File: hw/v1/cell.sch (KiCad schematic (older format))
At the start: 40 parts, among them Q201 Q_NMOS_GDS, Q202 Q_NMOS_GDS, Q203 Q_NMOS_GDS, U201 OPA1604, U202 ZTP-135SR

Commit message: Progress with the schema and PCB....
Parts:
- removed C209: 10n, Capacitor_SMD:C_0603_1608Metric, symbol Device:C_Small
- removed C210: 100n, Capacitor_SMD:C_0603_1608Metric, symbol Device:C_Small
- removed R213: 150, Resistor_SMD:R_0603_1608Metric, symbol Device:R_Small
- removed R215: 2k, Resistor_SMD:R_0603_1608Metric, symbol Device:R_Small
- removed U201: OPA1604, Package_SO:SOIC-16_3.9x9.9mm_P1.27mm, symbol Amplifier_Operational:OPA1604
- removed U202: ZTP-135SR, Package_TO_SOT_THT:TO-46-4_Window, symbol Cell_Shaper:ZTP-135SR
- added C209: 100n, Capacitor_SMD:C_0603_1608Metric, symbol Device:C
- added R218: 100k, Resistor_SMD:R_0603_1608Metric, symbol Device:R_Small
- added R219: 10k, Resistor_SMD:R_0603_1608Metric, symbol Device:R_Small
- added R220: 0, Resistor_SMD:R_0603_1608Metric, symbol Device:R
- added U201: MCP1416, Package_TO_SOT_SMD:SOT-23-5, symbol Driver_FET:MCP1416
- added U202: LMV344IPWR, Package_SO:TSSOP-14_4.4x5mm_P0.65mm, symbol Amplifier_Operational:LMV324
- C201, C202: value 10u -> 10u 16V
- C204: renamed from C203; value 10u -> 22u
- C205: renamed from C204; value 1u -> 10u
- C206: renamed from C205; DNP (none) -> DNP
- C207, C208: DNP (none) -> DNP
- D203: renamed from D202; value D_Schottky -> DFLS230Q; footprint Diode_SMD:D_0603_1608Metric -> Diode_SMD:D_PowerDI-123
- L201: value 10u -> 100u; footprint Inductor_SMD:L_Vishay_IHLP-2525 -> Inductor_SMD:L_Wuerth_HCI-7050
- Q201: value Q_NMOS_GDS -> ZVN4206G; footprint Package_TO_SOT_SMD:SOT-223 -> Package_TO_SOT_SMD:SOT-223-3_TabPin2
- Q202, Q203: value Q_NMOS_GDS -> IRFZ24NPbF
- R203: renamed from R201; value R -> 10k
- R204: renamed from R202; value 1k -> 22k 0.5%
- R205: renamed from R203; value 1k -> 1k 0.5%
- R206: renamed from R204; value 0R1 -> 0R1 1%; footprint Resistor_SMD:R_1210_3225Metric -> Resistor_SMD:R_1206_3216Metric
- R207: renamed from R205; value 1k -> 1k 0.5%
- R208: renamed from R219; value 1k -> 22k 0.5%
- R209: renamed from R218; value R -> 10k
- R210: renamed from R206; value 0R1 -> 0R1 1%; footprint Resistor_SMD:R_1210_3225Metric -> Resistor_SMD:R_1206_3216Metric
- R211: renamed from R208; value 1k -> 1k 0.5%
- R212: renamed from R209; value 1k -> 1k 0.5%
- R213: renamed from R207; value 1k -> 100
- R214: renamed from R210; value 1k -> 200k
- R215: renamed from R211; DNP (none) -> DNP
- R216: renamed from R212; value 1k -> 22k 0.5%
- R217: renamed from R214; value 18k -> 1k
- TH201: footprint (none) -> CellShaper:ContactThermistor
- renumbered C206 to C203, D203 to D202, R216 to R201, R217 to R202
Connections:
- net labels added: CELL_POSITIVE, GATE, GNDPWR
- net labels removed: CELL
- wire segments 114 -> 120
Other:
- note added: "1A = 2.3V"
- note added: "? mA/mV"
- note added: "Cell temperature"
- note added: "Charge current\nmeasurement"
- note added: "Max 5V"
- note added: "TODO: Is it possible to make 4-wire voltage measurement? \nNow possible voltage difference between\nGND and PWR GND is added to measurement!\n\nChange opamp VCC to regulated 5V and use opamp\nas differential amp and have divider on output?"
- note added: "TODO: Single two-color LED?"
- note added: "Up to 2A and 12V"
- note added: "Wire leaded NTC\non a foam pad"
- note removed: "(Opamp is not really needed but\nquad packaged opamps are so common)"
- note removed: "Cel temperature"
- note removed: "Charge current measurement"
- note removed: "If DAC is used no filtering here!"
- moved on the sheet: BT201, C201, C202, C203, C204, C205, C206, C207, C208, D201, D202, D203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

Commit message: Progress...
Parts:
- added R221, R222: 300k 0.5%, Resistor_SMD:R_0603_1608Metric, symbol Device:R_Small
- added R223: 100k 0.5%, Resistor_SMD:R_0603_1608Metric, symbol Device:R_Small
- R214: value 200k -> 100k 0.5%
- R218: value 100k -> 100k 0.5%
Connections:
- net CELL_POSITIVE: now also R221.1; no longer R218.1
- net CELL_VOLTAGE: now also R218.1; no longer U202.2 (-)
- net GND: now also R214.1, R223.1
- net GNDPWR: now also R222.1; no longer R214.2
- net at C207.2, R211.2, U202.5 (+): now also R223.2
- new net: R214.2, R221.2, U202.3 (+)
- new net: R218.2, R222.2, U202.2 (-)
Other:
- note added: "3.3V --> 1.6A\n? mA/mV"
- note added: "Difference amplifier"
- note added: "Discharge current control"
- note added: "gain = 0.33333"
- note removed: "? mA/mV"
- note removed: "TODO: Is it possible to make 4-wire voltage measurement? \nNow possible voltage difference between\nGND and PWR GND is added to measurement!\n\nChange opamp VCC to regulated 5V and use opamp\nas differential amp and have divider on output?"
- moved on the sheet: R314, R318, U302A

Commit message: Soon...
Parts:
- added NT501: Net-Tie_2, NetTie:NetTie-2_SMD_Pad0.5mm, symbol Device:Net-Tie_2
- L201: footprint Inductor_SMD:L_Wuerth_HCI-7050 -> Inductor_SMD:L_Wuerth_HCM-1052
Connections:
- net CELL_VOLTAGE: now also U202.14; no longer U202.1
- net CHARGE_CURRENT: now also U202.1; no longer U202.14
- net GNDPWR: now also NT501.1; no longer R222.1
- net at C206.1, R204.2, R207.1: now also U202.2 (-); no longer U202.13 (-)
- net at C206.2, R205.1, R208.2: now also U202.3 (+); no longer U202.12 (+)
- net at R214.2, R221.2: now also U202.12 (+); no longer U202.3 (+)
- net at R218.2, R222.2: now also U202.13 (-); no longer U202.2 (-)
- new net: NT501.2, R222.1
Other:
- moved on the sheet: R221, R222, U202A, U202D

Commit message: Soooooon...
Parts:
- added R19, R5: 200m 1%, Resistor_SMD:R_1206_3216Metric, symbol Device:R
- R20: renamed from R210; value 0R1 1% -> 200m 1%
- R6: renamed from R206; value 0R1 1% -> 200m 1%
- renumbered BT201 to BT1, C201 to C1, C202 to C2, C204 to C3, C205 to C4, C206 to C5, C208 to C6, C209 to C7, C207 to C8, C203 to C9, D203 to D1, D201 to D2, D202 to D3, L201 to L1, NT501 to NT5, Q201 to Q1, Q203 to Q2, Q202 to Q3, R214 to R1, R213 to R10, R219 to R11, R220 to R12, R215 to R13, R208 to R14, R204 to R15, R203 to R16, R223 to R17, R211 to R18, R221 to R2, R212 to R21, R216 to R22, R209 to R23, R201 to R24, R202 to R25, R222 to R3, R218 to R4, R205 to R7, R207 to R8, R217 to R9, TH201 to TH1, U202 to U1, U201 to U2
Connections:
- net CELL_POSITIVE: now also R5.2
- net GNDPWR: now also R19.2
- net at Q2.3 (S), Q3.3 (S), R18.1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: now also R19.1
- net at C3.1, C4.1, L1.2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: now also R5.1
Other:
- note added: "Charge current shunt\n2x 200m or 1x 100m"
- note added: "Discharge current shunt\n2x 200m or 1x 100m"
- note removed: "Charge current\nmeasurement"

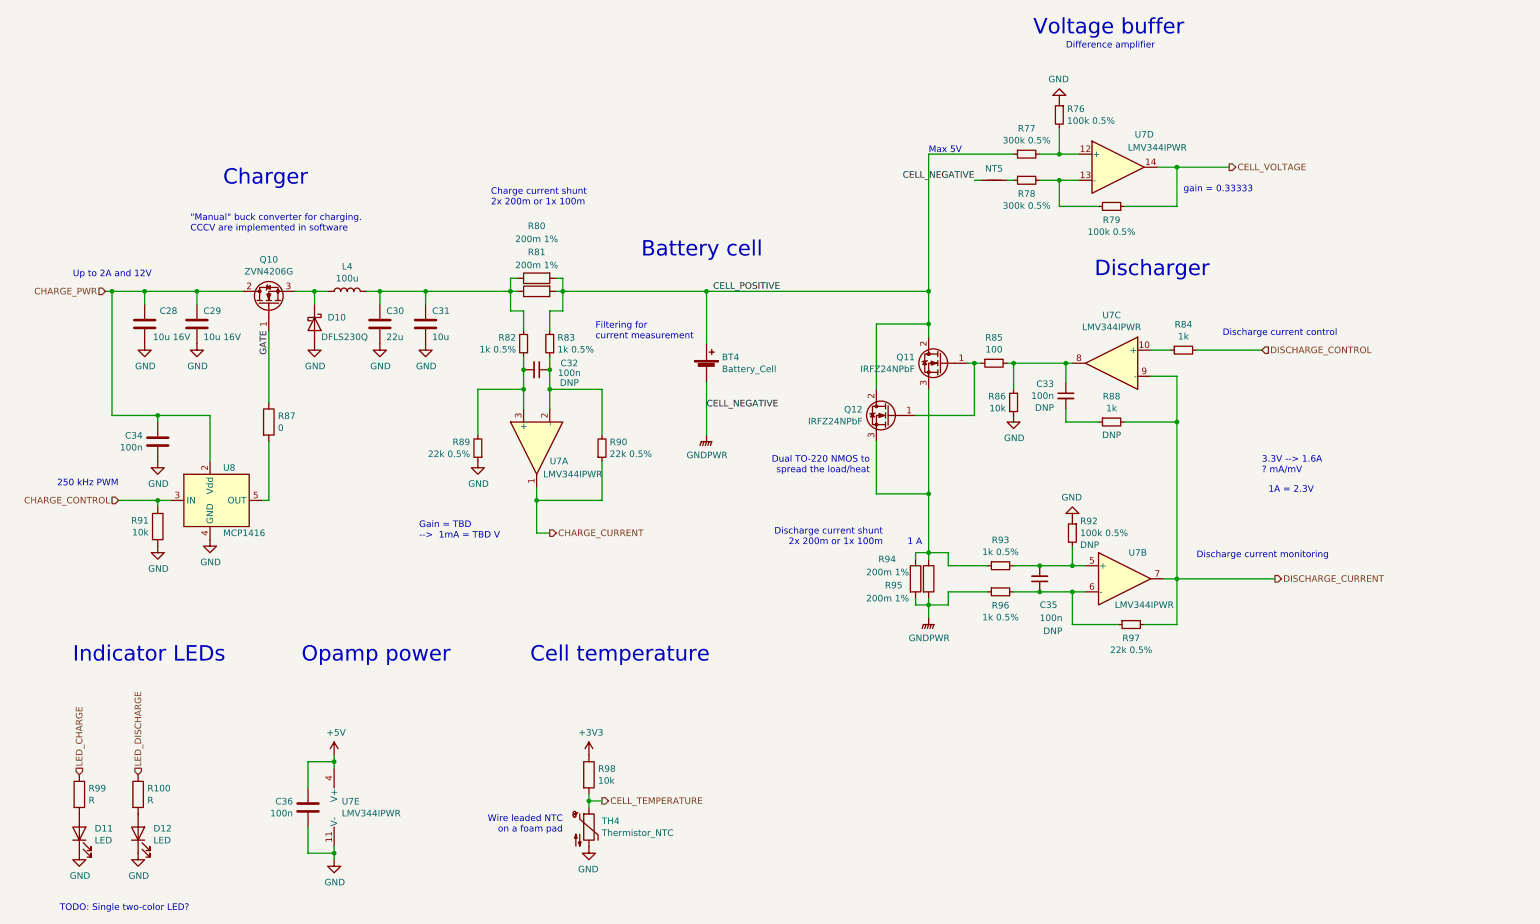
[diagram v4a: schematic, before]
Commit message: Layout done and MCU pins rearranged
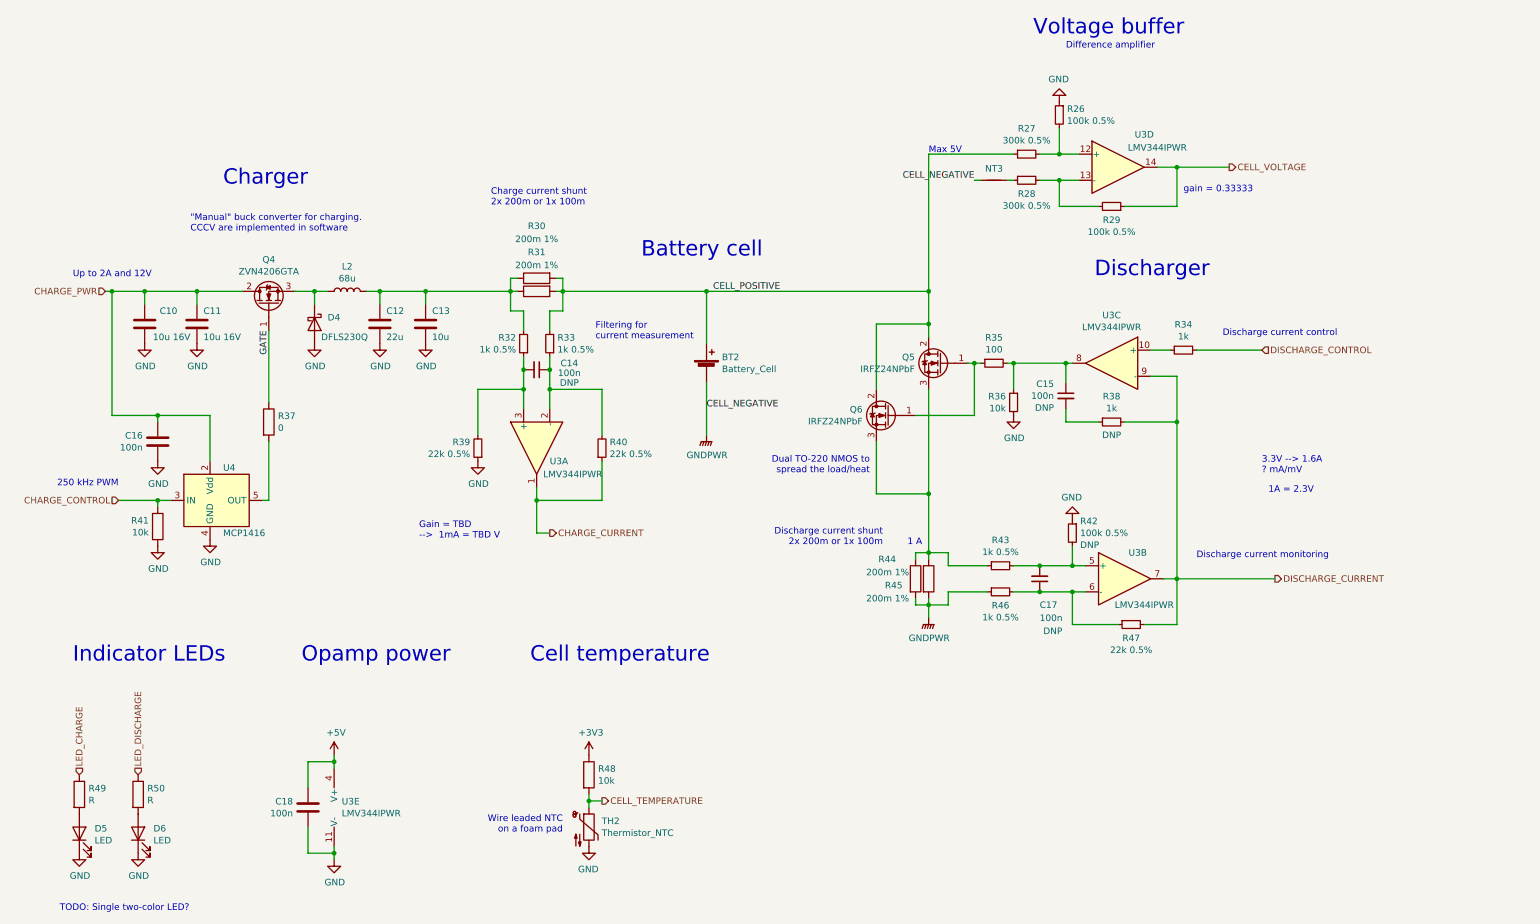
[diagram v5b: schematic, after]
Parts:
- L1: value 100u -> 68u
- Q1: value ZVN4206G -> ZVN4206GTA
